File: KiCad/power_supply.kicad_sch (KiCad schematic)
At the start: 9 parts, among them SW1 SW_Push, U1 STM32F401RBTx, Y1 26MHz

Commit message: Ki cad schematic update.
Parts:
- added C10, C13, C3, C4, C5, C6, C7, C8, C9: 100nF, symbol Device:C
- added C16: 4uF7, symbol Device:C
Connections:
- net GND: now also C10.2, C13.2, C16.2, C3.2, C4.2, C5.2, C6.2, C7.2, C8.2, C9.2
- net BTN_DWN: no longer names the net of U1.28 (PB2)
- net BTN_UP: no longer names the net of U1.27 (PB1)
- net VDD renamed +3.3V
- net +3.3V: now also C10.1, C13.1, C16.1, C3.1, C4.1, C5.1, C6.1, C7.1, C8.1, C9.1
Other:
- sheet VDD renamed Main_Supply
- removed sheet LCD
- sheet Main_Supply: file VDD.kicad_sch -> Main_Supply.kicad_sch
- note added: "To Mcu"
- note removed: "Debounce"

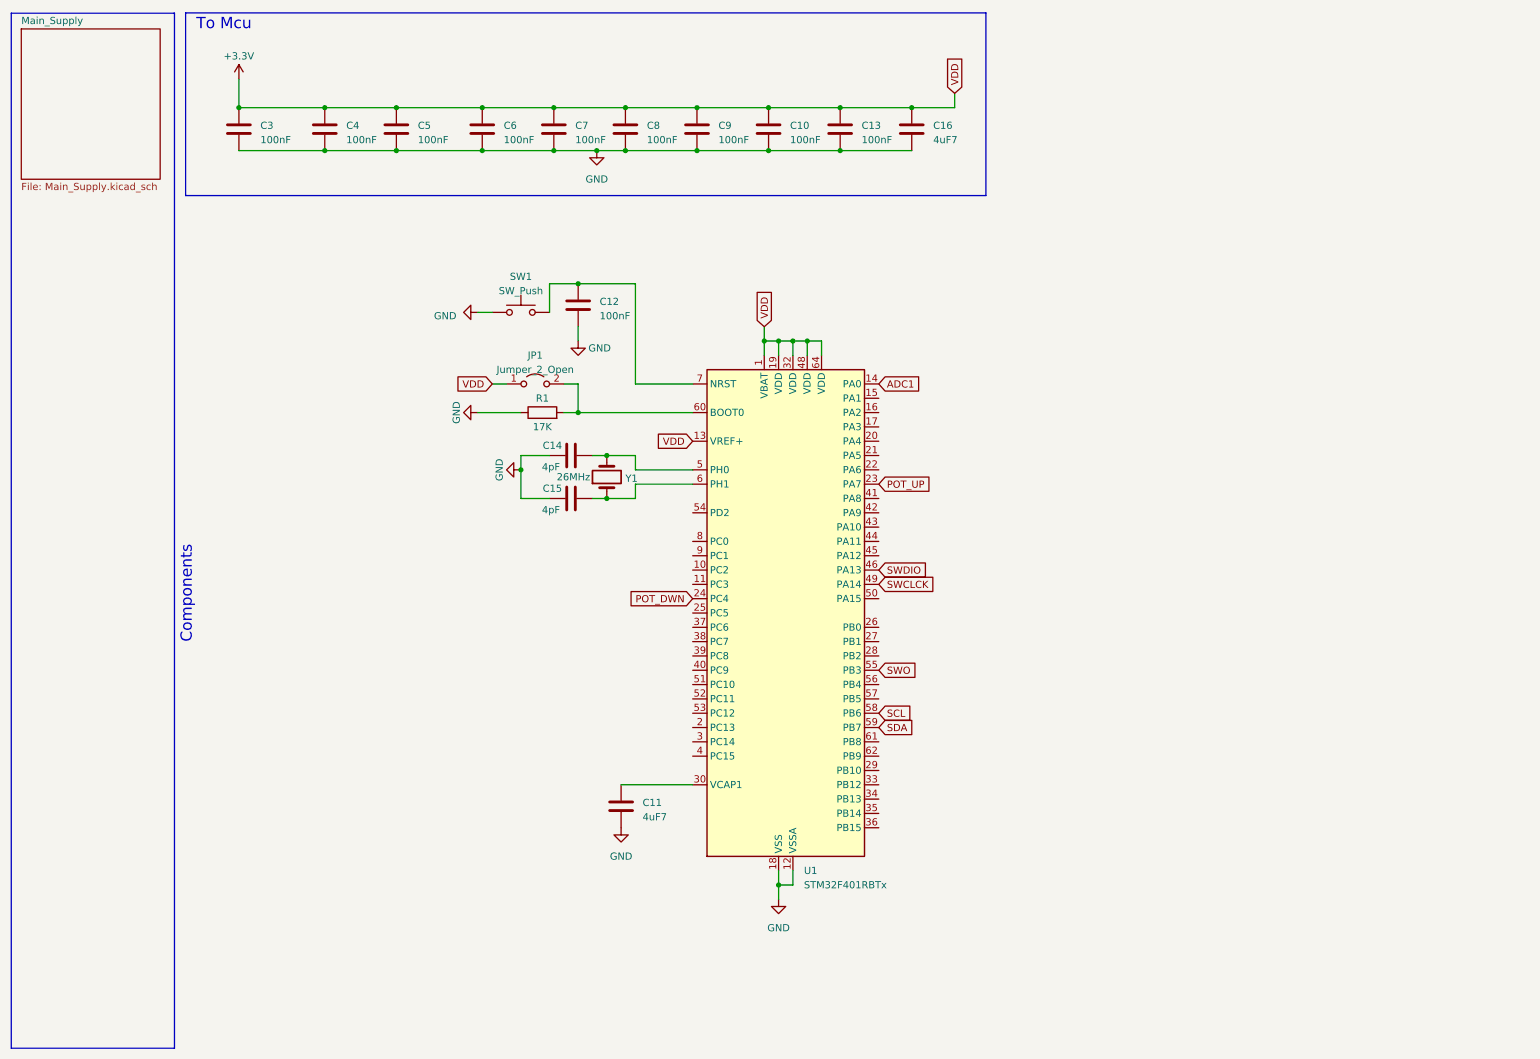
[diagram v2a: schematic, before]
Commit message: Schematics updated. footprint assignment and layout still needed
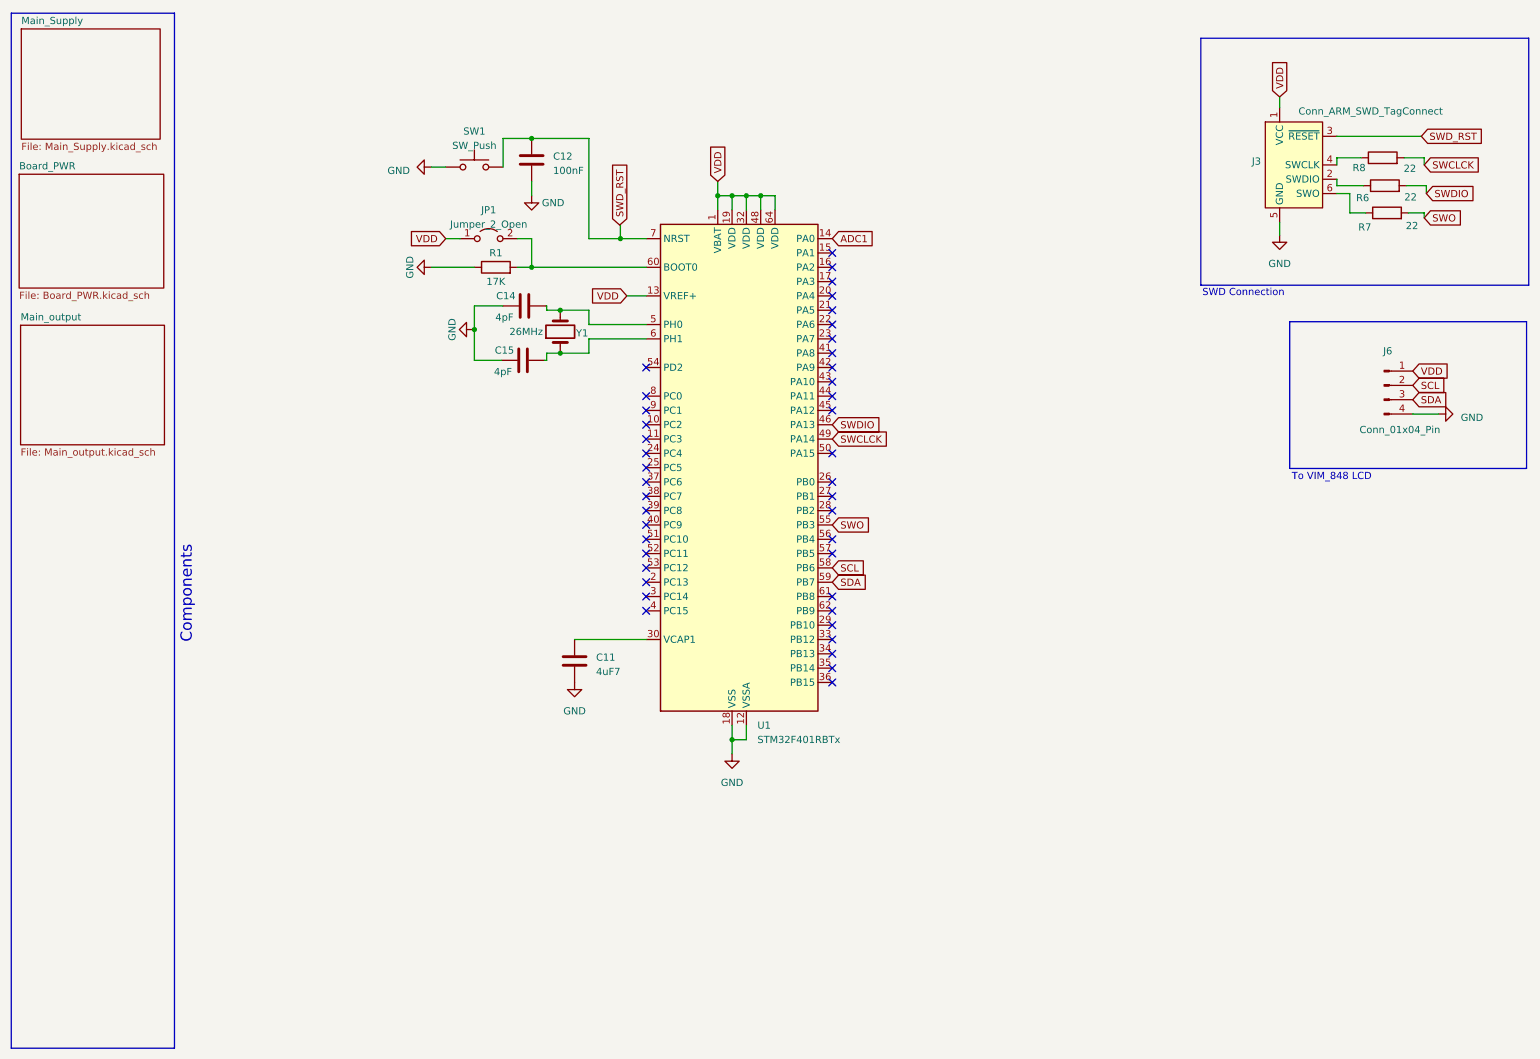
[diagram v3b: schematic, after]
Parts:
- removed C10, C13, C3, C4, C5, C6, C7, C8, C9: 100nF, symbol Device:C
- removed C16: 4uF7, symbol Device:C
- added J3: Conn_ARM_SWD_TagConnect, Connector:Tag-Connect_TC2030-IDC-NL_2x03_P1.27mm_Vertical, symbol Connector:Conn_ARM_SWD_TagConnect_TC2030-NL
- added J6: Conn_01x04_Pin, symbol Connector:Conn_01x04_Pin
- added R6, R7, R8: 22, symbol Device:R
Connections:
- net GND: now also J3.5 (GND), J6.4 (Pin_4)
- net SCL: now also J6.2 (Pin_2)
- net SDA: now also J6.3 (Pin_3)
- net SWCLCK: now also R8.2
- net SWDIO: now also R6.2
- net SWO: now also R7.2
- net SWD_RST: now reaches C12.1, SW1.2, U1.7 (NRST)
- net SWD_RST: now also J3.3 (~{RESET})
- net +3.3V renamed VDD
- net VDD: now also J3.1 (VCC), J6.1 (Pin_1)
- net POT_DWN: no longer names the net of U1.24 (PC4)
- net POT_UP: no longer names the net of U1.23 (PA7)
- new net: J3.6 (SWO), R7.1
- new net: J3.2 (SWDIO), R6.1
- new net: J3.4 (SWCLK), R8.1
- no-connect marks 0 -> 42
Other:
- added sheet Board_PWR (Board_PWR.kicad_sch)
- added sheet Main_output (Main_output.kicad_sch)
- note added: "SWD Connection"
- note added: "To VIM_848 LCD"
- note removed: "To Mcu"
- moved on the sheet: C11, C12, C14, C15, JP1, R1, SW1, U1, Y1
